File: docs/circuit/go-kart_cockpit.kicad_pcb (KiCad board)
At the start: 2 copper layers, 103.5 x 57.2 mm, 37 parts, among them P1 Power, Q1 TIP120, X1 Taster rechts (male), X10 Bluetooth-Modul, X11 Display (male), X12 PD7, X13 SDA, X14 PG4, X15 AVR-ISP-10, X16 Taster links (male), X17 Start/Stop/Rückwärts, X2 5V, X3 GND, X4 24V Hupe, X5 SCL, X6 CS, X7 PB6, X8 J5, X9 J3

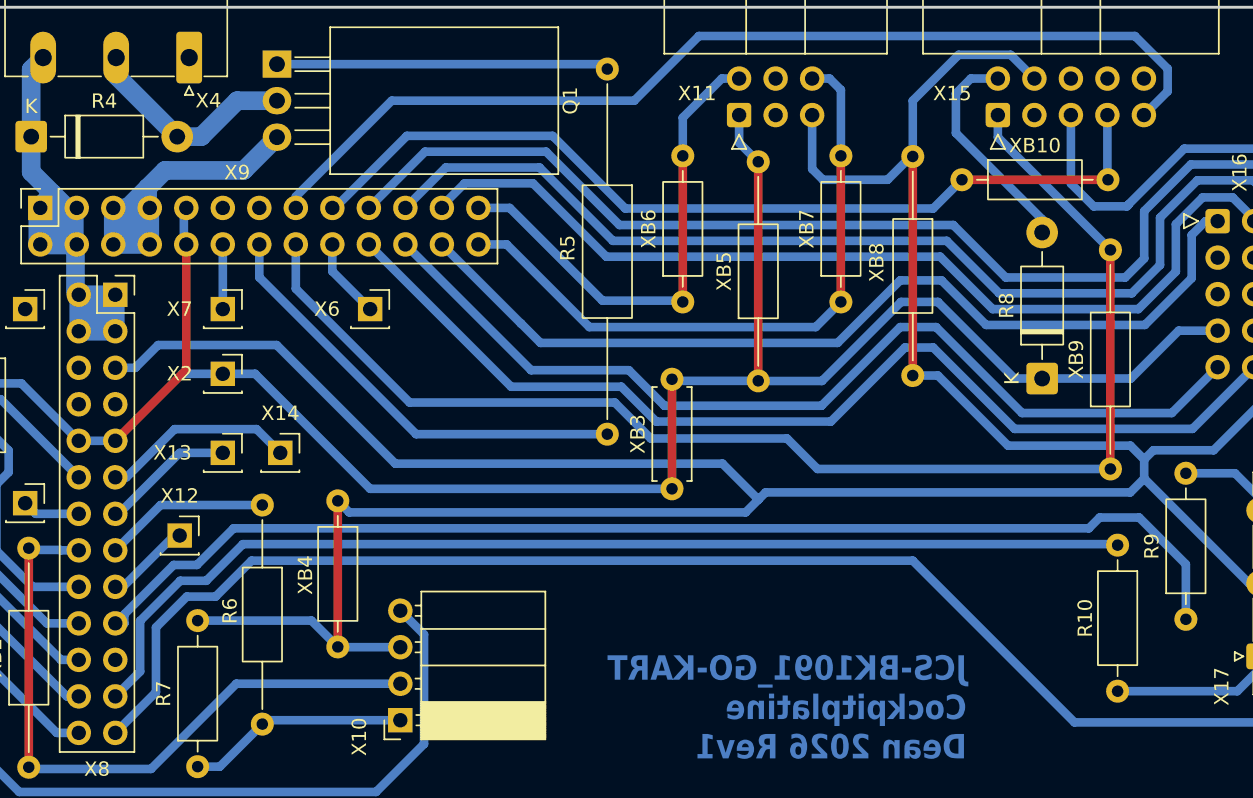
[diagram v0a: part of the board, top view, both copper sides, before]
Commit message: feat(PCB): add pull down resistor in preperation for FET
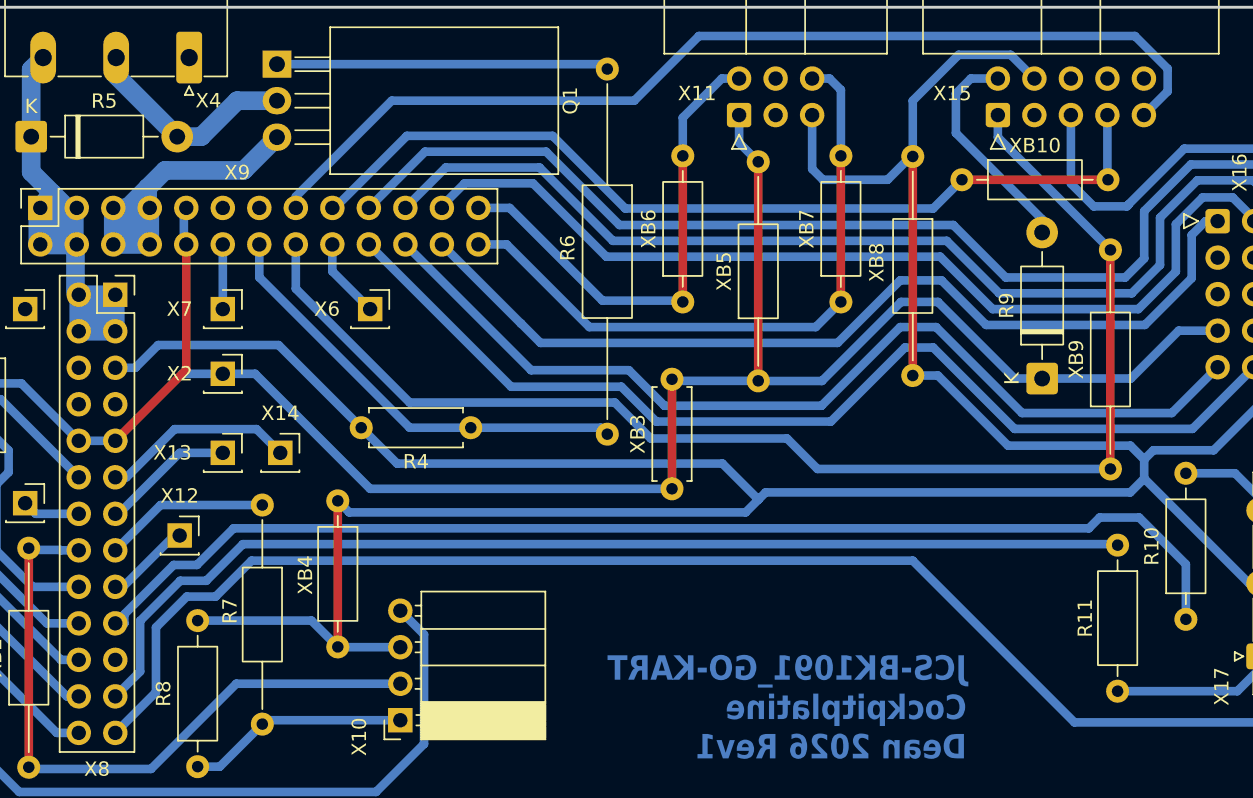
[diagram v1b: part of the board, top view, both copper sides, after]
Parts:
- added R4: 10k, Resistor_THT:R_Axial_DIN0207_L6.3mm_D2.5mm_P7.62mm_Horizontal, F.Cu at (98.5, 76.8)
- renumbered R9 to R10, R10 to R11, R4 to R5, R5 to R6, R6 to R7, R7 to R8, R8 to R9
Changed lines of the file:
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@@
 	(net 36 "/PG4")
 	(net 37 "/PB0_CS")
-	(net 38 "Net-(R8-A)")
-	(net 39 "Net-(R10-Pad2)")
+	(net 38 "Net-(R9-A)")
+	(net 39 "Net-(R11-Pad2)")
 	(net 40 "unconnected-(X1-Pin_4-Pad4)")
 	(net 41 "unconnected-(X1-Pin_6-Pad6)")
@@
 		(descr "Resistor, Axial_DIN0207 series, Axial, Horizontal, pin pitch=10.16mm, 0.25W = 1/4W, length*diameter=6.3*2.5mm^2, http://cdn-reichelt.de/documents/datenblatt/B400/1_4W%23YAG.pdf")
 		(tags "Resistor Axial_DIN0207 series Axial Horizontal pin pitch 10.16mm 0.25W = 1/4W length 6.3mm diameter 2.5mm")
-		(property "Reference" "R7"
+		(property "Reference" "R8"
 			(at 5.08 -2.37 90)
 			(layer "F.SilkS")
@@
 		(descr "Resistor, Axial_DIN0207 series, Axial, Horizontal, pin pitch=15.24mm, 0.25W = 1/4W, length*diameter=6.3*2.5mm^2, http://cdn-reichelt.de/documents/datenblatt/B400/1_4W%23YAG.pdf")
 		(tags "Resistor Axial_DIN0207 series Axial Horizontal pin pitch 15.24mm 0.25W = 1/4W length 6.3mm diameter 2.5mm")
-		(property "Reference" "R6"
+		(property "Reference" "R7"
 			(at 7.37 2.25 270)
 			(layer "F.SilkS")
@@
 		(descr "Diode, DO-41_SOD81 series, Axial, Horizontal, pin pitch=10.16mm, length*diameter=5.2*2.7mm^2, https://www.diodes.com/assets/Package-Files/DO-41-Plastic.pdf")
 		(tags "Diode DO-41_SOD81 series Axial Horizontal pin pitch 10.16mm  length 5.2mm diameter 2.7mm")
-		(property "Reference" "R4"
+		(property "Reference" "R5"
 			(at 5.08 -2.47 0)
 			(layer "F.SilkS")
@@
 		(descr "Resistor, Axial_DIN0207 series, Axial, Horizontal, pin pitch=10.16mm, 0.25W = 1/4W, length*diameter=6.3*2.5mm^2, http://cdn-reichelt.de/documents/datenblatt/B400/1_4W%23YAG.pdf")
 		(tags "Resistor Axial_DIN0207 series Axial Horizontal pin pitch 10.16mm 0.25W = 1/4W length 6.3mm diameter 2.5mm")
-		(property "Reference" "R10"
+		(property "Reference" "R11"
 			(at 5.08 2.25 270)
 			(layer "F.SilkS")
@@
 			(layers "*.Cu" "*.Mask")
 			(remove_unused_layers no)
-			(net 39 "Net-(R10-Pad2)")
+			(net 39 "Net-(R11-Pad2)")
 			(pintype "passive")
 		)
@@
 		(descr "Resistor, Axial_DIN0207 series, Axial, Horizontal, pin pitch=10.16mm, 0.25W = 1/4W, length*diameter=6.3*2.5mm^2, http://cdn-reichelt.de/documents/datenblatt/B400/1_4W%23YAG.pdf")
 		(tags "Resistor Axial_DIN0207 series Axial Horizontal pin pitch 10.16mm 0.25W = 1/4W length 6.3mm diameter 2.5mm")
-		(property "Reference" "R9"
+		(property "Reference" "R10"
 			(at 5.08 -2.37 90)
 			(layer "F.SilkS")
@@
 		(descr "Resistor, Axial_DIN0309 series, Axial, Horizontal, pin pitch=25.4mm, 0.5W = 1/2W, length*diameter=9*3.2mm^2, http://cdn-reichelt.de/documents/datenblatt/B400/1_4W%23YAG.pdf")
 		(tags "Resistor Axial_DIN0309 series Axial Horizontal pin pitch 25.4mm 0.5W = 1/2W length 9mm diameter 3.2mm")
-		(property "Reference" "R5"
+		(property "Reference" "R6"
 			(at 12.45 2.75 270)
 			(layer "F.SilkS")
@@
 			(remove_unused_layers no)
 			(roundrect_rratio 0.138889)
-			(net 39 "Net-(R10-Pad2)")
+			(net 39 "Net-(R11-Pad2)")
 			(pinfunction "1")
 			(pintype "passive")
@@
 		)
 	)
+	(footprint "Resistor_THT:R_Axial_DIN0207_L6.3mm_D2.5mm_P7.62mm_Horizontal"
+		(layer "F.Cu")
+		(at 98.5 76.75 180)
+		(descr "Resistor, Axial_DIN0207 series, Axial, Horizontal, pin pitch=7.62mm, 0.25W = 1/4W, length*diameter=6.3*2.5mm^2, http://cdn-reichelt.de/documents/datenblatt/B400/1_4W%23YAG.pdf")
+		(tags "Resistor Axial_DIN0207 series Axial Horizontal pin pitch 7.62mm 0.25W = 1/4W length 6.3mm diameter 2.5mm")
+		(property "Reference" "R4"
+			(at 3.81 -2.37 0)
+			(layer "F.SilkS")
+			(effects
+				(font
+					(size 1 1)
+					(thickness 0.15)
+				)
+			)
+		)
+		(property "Value" "10k"
+			(at 3.81 2.37 0)
+			(layer "F.Fab")
+			(effects
+				(font
+					(size 1 1)
+					(thickness 0.15)
+				)
+			)
+		)
+		(property "Datasheet" "~"
+			(at 0 0 0)
+			(layer "F.Fab")
+			(hide yes)
+			(effects
+				(font
+					(size 1.27 1.27)
+					(thickness 0.15)
+				)
+			)
+		)
+		(property "Description" "Resistor"
+			(at 0 0 0)
+			(layer "F.Fab")
+			(hide yes)
+			(effects
+				(font
+					(size 1.27 1.27)
+					(thickness 0.15)
+				)
+			)
+		)
+		(property ki_fp_filters "R_*")
+		(sheetname "/")
+		(sheetfile "go-kart_cockpit.kicad_sch")
+		(attr through_hole)
+		(fp_line
+			(start 7.08 1.37)
+			(end 7.08 1.04)
+			(stroke
+				(width 0.12)
+				(type solid)
+			)
+			(layer "F.SilkS")
+		)
+		(fp_line
+			(start 7.08 -1.37)
+			(end 7.08 -1.04)
+			(stroke
+				(width 0.12)
+				(type solid)
+			)
+			(layer "F.SilkS")
+		)
+		(fp_line
+			(start 0.54 1.37)
+			(end 7.08 1.37)
+			(stroke
+				(width 0.12)
+				(type solid)
+			)
+			(layer "F.SilkS")
+		)
+		(fp_line
+			(start 0.54 1.04)
+			(end 0.54 1.37)
+			(stroke
+				(width 0.12)
+				(type solid)
+			)
+			(layer "F.SilkS")
+		)
+		(fp_line
+			(start 0.54 -1.04)
+			(end 0.54 -1.37)
+			(stroke
+				(width 0.12)
+				(type solid)
+			)
+			(layer "F.SilkS")
+		)
+		(fp_line
+			(start 0.54 -1.37)
+			(end 7.08 -1.37)
+			(stroke
+				(width 0.12)
+				(type solid)
+			)
+			(layer "F.SilkS")
+		)
+		(fp_rect
+			(start -1.05 -1.5)
+			(end 8.67 1.5)
+			(stroke
+				(width 0.05)
+				(type solid)
+			)
+			(fill no)
+			(layer "F.CrtYd")
+		)
+		(fp_line
+			(start 7.62 0)
+			(end 6.96 0)
+			(stroke
+				(width 0.1)
+				(type solid)
+			)
+			(layer "F.Fab")
+		)
+		(fp_line
+			(start 0 0)
+			(end 0.66 0)
+			(stroke
+				(width 0.1)
+				(type solid)
+			)
+			(layer "F.Fab")
+		)
+		(fp_rect
+			(start 0.66 -1.25)
+			(end 6.96 1.25)
+			(stroke
+				(width 0.1)
+				(type solid)
+			)
+			(fill no)
+			(layer "F.Fab")
+		)
+		(fp_text user "${REFERENCE}"
+			(at 3.81 0 0)
+			(layer "F.Fab")
+			(effects
+				(font
+					(size 1 1)
+					(thickness 0.15)
+				)
+			)
+		)
+		(pad "1" thru_hole circle
+			(at 0 0 180)
+			(size 1.6 1.6)
+			(drill 0.8)
+			(layers "*.Cu" "*.Mask")
+			(remove_unused_layers no)
+			(net 30 "PB4_OC2A")
+			(pintype "passive")
+		)
+		(pad "2" thru_hole circle
+			(at 7.62 0 180)
+			(size 1.6 1.6)
+			(drill 0.8)
+			(layers "*.Cu" "*.Mask")
+			(remove_unused_layers no)
+			(net 2 "GND")
+			(pintype "passive")
+		)
+		(embedded_fonts no)
+		(model "${KICAD9_3DMODEL_DIR}/Resistor_THT.3dshapes/R_Axial_DIN0207_L6.3mm_D2.5mm_P7.62mm_Horizontal.step"
+			(offset
+				(xyz 0 0 0)
+			)
+			(scale
+				(xyz 1 1 1)
+			)
+			(rotate
+				(xyz 0 0 0)
+			)
+		)
+	)
 	(footprint "Diode_THT:D_DO-41_SOD81_P10.16mm_Horizontal"
 		(layer "F.Cu")
@@
 		(descr "Diode, DO-41_SOD81 series, Axial, Horizontal, pin pitch=10.16mm, length*diameter=5.2*2.7mm^2, https://www.diodes.com/assets/Package-Files/DO-41-Plastic.pdf")
 		(tags "Diode DO-41_SOD81 series Axial Horizontal pin pitch 10.16mm  length 5.2mm diameter 2.7mm")
-		(property "Reference" "R8"
+		(property "Reference" "R9"
 			(at 5.08 -2.47 90)
 			(layer "F.SilkS")
@@
 			(layers "*.Cu" "*.Mask")
 			(remove_unused_layers no)
-			(net 38 "Net-(R8-A)")
+			(net 38 "Net-(R9-A)")
 			(pinfunction "A")
 			(pintype "passive")
@@
 			(layers "*.Cu" "*.Mask")
 			(remove_unused_layers no)
-			(net 38 "Net-(R8-A)")
+			(net 38 "Net-(R9-A)")
 			(pinfunction "VCC")
 			(pintype "passive")
@@
 	)
 	(segment
-		(start 93.25 79.25)
-		(end 85 71)
+		(start 154.651 71.651)
+		(end 154.651 73.849)
 		(width 0.6)
 		(layer "B.Cu")
@@
 	)
 	(segment
-		(start 154.651 71.651)
-		(end 154.651 73.849)
+		(start 116.009156 79.245)
+		(end 118.514156 81.75)
 		(width 0.6)
 		(layer "B.Cu")
@@
 	)
 	(segment
+		(start 90.88 76.75)
+		(end 85.13 71)
+		(width 0.6)
+		(layer "B.Cu")
+		(net 2)
+	)
+	(segment
 		(start 64.71 78.96)
 		(end 64.75 79)
@@
 	)
 	(segment
-		(start 85 71)
-		(end 76.75 71)
-		(width 0.6)
-		(layer "B.Cu")
-		(net 2)
-	)
-	(segment
 		(start 154.651 73.849)
 		(end 150.181 78.319)
@@
 	)
 	(segment
-		(start 76.75 71)
-		(end 75.17 72.58)
-		(width 0.6)
+		(start 73.63 64)
+		(end 76.17 61.46)
+		(width 1.3)
 		(layer "B.Cu")
 		(net 2)
 	)
 	(segment
-		(start 73.63 64)
-		(end 76.17 61.46)
-		(width 1.3)
+		(start 76.75 71)
+		(end 75.17 72.58)
+		(width 0.6)
 		(layer "B.Cu")
 		(net 2)
@@
 	)
 	(segment
-		(start 116.014156 79.25)
-		(end 93.25 79.25)
+		(start 65 71.5)
+		(end 65 71.44)
 		(width 0.6)
 		(layer "B.Cu")
@@
 	)
 	(segment
-		(start 65 71.5)
-		(end 65 71.44)
+		(start 93.375 79.245)
+		(end 116.009156 79.245)
 		(width 0.6)
 		(layer "B.Cu")
@@
 	)
 	(segment
-		(start 118.514156 81.75)
-		(end 116.014156 79.25)
-		(width 0.6)
-		(layer "B.Cu")
-		(net 2)
-	)
-	(segment
 		(start 150.181 78.319)
 		(end 145.988844 78.319)
@@
 	)
 	(segment
+		(start 90.88 76.75)
+		(end 93.375 79.245)
+		(width 0.6)
+		(layer "B.Cu")
+		(net 2)
+	)
+	(segment
 		(start 119.014156 81.25)
 		(end 118.514156 81.75)
@@
 	)
 	(segment
+		(start 85.13 71)
+		(end 76.75 71)
+		(width 0.6)
+		(layer "B.Cu")
+		(net 2)
+	)
+	(segment
 		(start 71.23 72.58)
 		(end 71.15 72.5)
@@
 	)
 	(segment
+		(start 75.17 72.58)
+		(end 73.77 72.58)
+		(width 0.6)
+		(layer "B.Cu")
+		(net 2)
+	)
+	(segment
 		(start 82.709 58.851)
 		(end 77.227 58.851)
@@
 	)
 	(segment
-		(start 75.17 72.58)
-		(end 73.77 72.58)
-		(width 0.6)
-		(layer "B.Cu")
-		(net 2)
-	)
-	(segment
 		(start 85.14 51.34)
 		(end 85.02 51.46)
@@
 	)
 	(segment
-		(start 83.79 64)
+		(start 107.55 76.75)
+		(end 108 77.2)
+		(width 0.6)
+		(layer "B.Cu")
+		(net 30)
+	)
+	(segment
+		(start 94.25 76.75)
 		(end 83.79 66.29)
 		(width 0.6)
@@
 	(segment
 		(start 83.79 66.29)
-		(end 94.7 77.2)
+		(end 83.79 64)
 		(width 0.6)
 		(layer "B.Cu")
@@
 	)
 	(segment
-		(start 94.7 77.2)
-		(end 108 77.2)
+		(start 98.5 76.75)
+		(end 94.25 76.75)
+		(width 0.6)
+		(layer "B.Cu")
+		(net 30)
+	)
+	(segment
+		(start 98.5 76.75)
+		(end 107.55 76.75)
 		(width 0.6)
 		(layer "B.Cu")

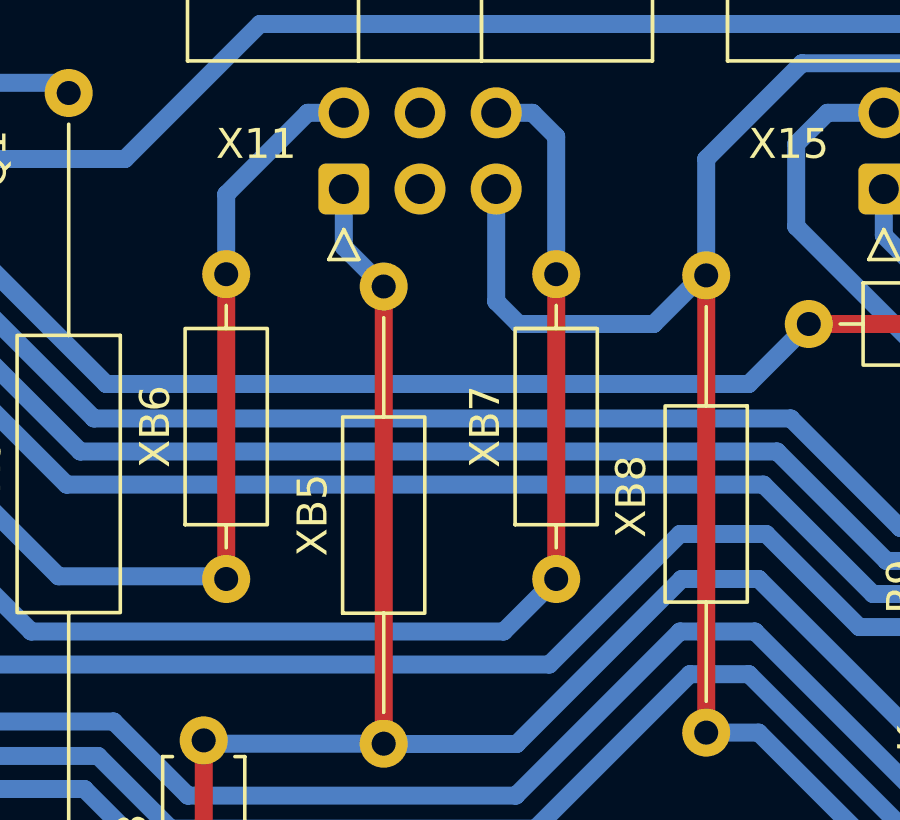
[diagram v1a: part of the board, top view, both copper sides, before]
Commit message: feat(PCB): add teardrops
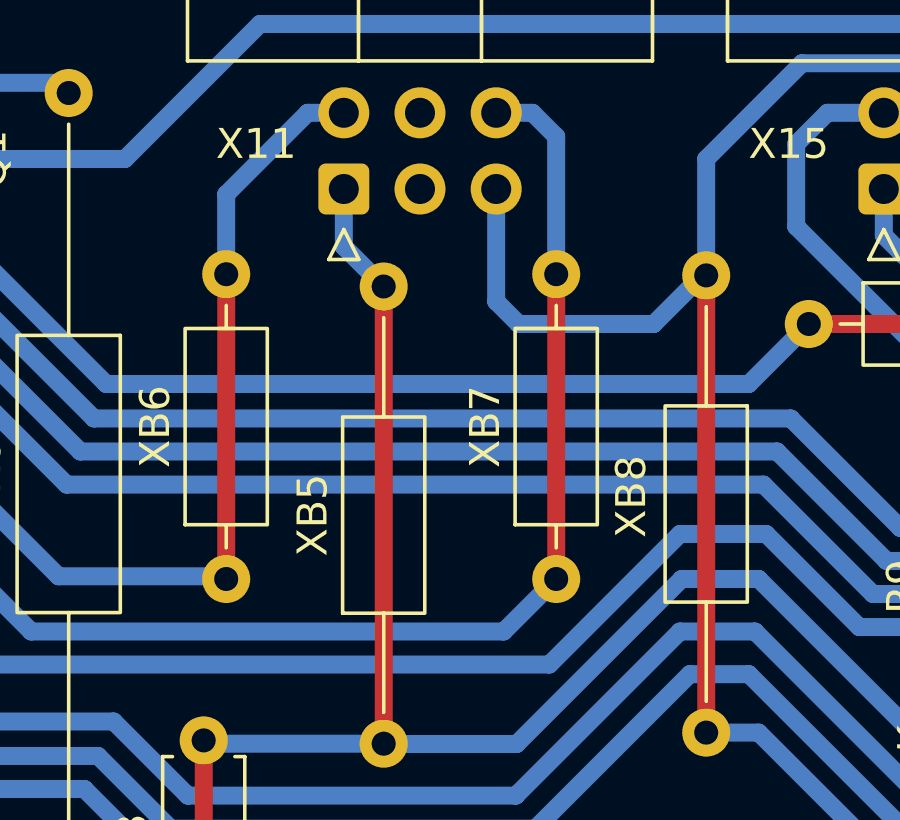
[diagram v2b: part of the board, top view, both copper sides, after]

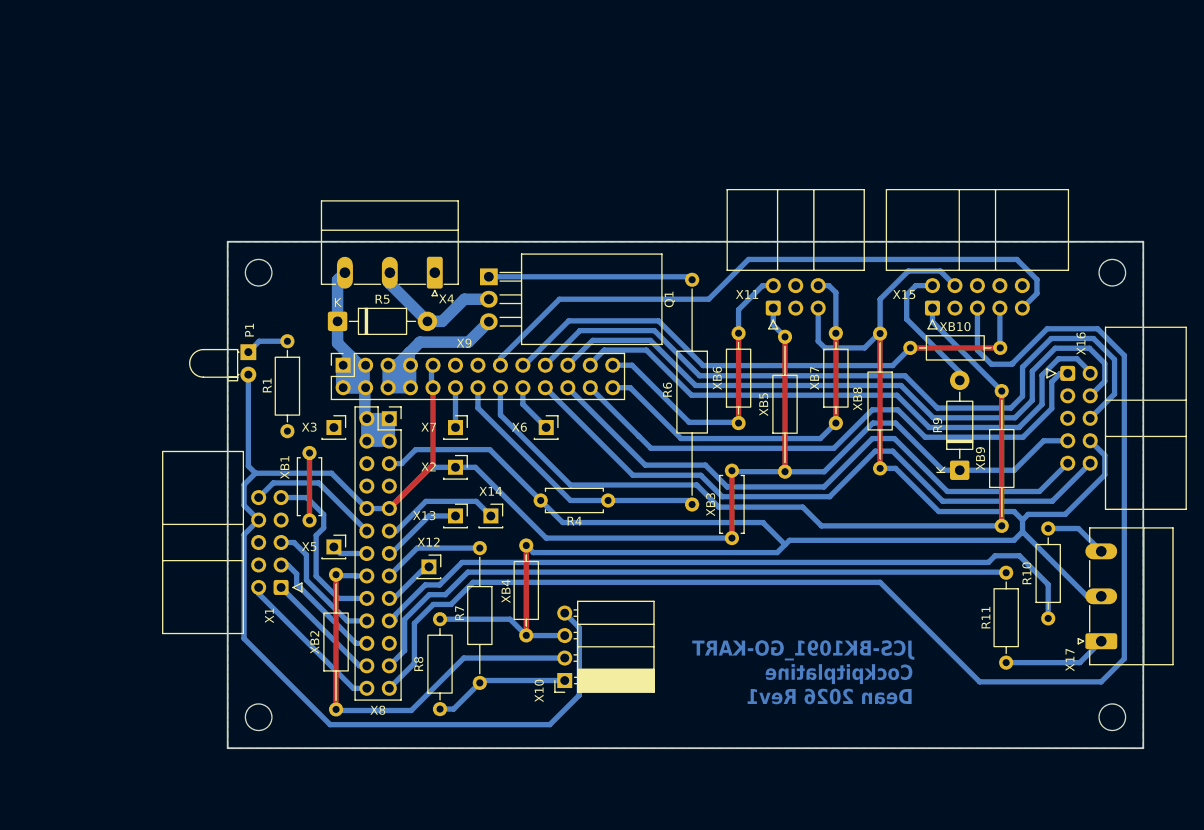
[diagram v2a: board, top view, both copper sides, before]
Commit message: feat(PCB): improve connectors and position
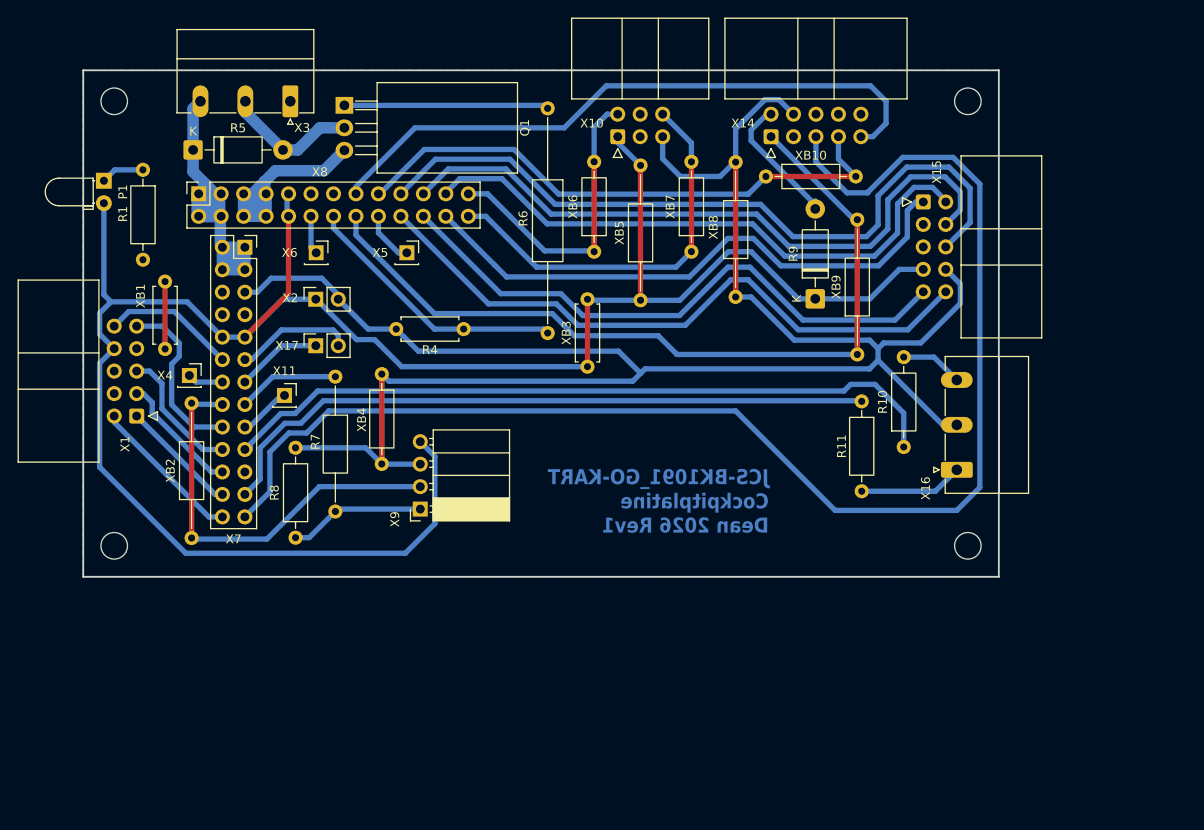
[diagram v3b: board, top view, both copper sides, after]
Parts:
- removed X13: SDA, Connector_PinSocket_2.54mm:PinSocket_1x01_P2.54mm_Vertical
- removed the X14 at (85.2, 78.5)
- removed the X3 at (67.5, 68.5)
- added X17: SDA PG4, Connector_PinSocket_2.54mm:PinSocket_1x02_P2.54mm_Vertical, F.Cu at (65.5, 59.2)
- X2: value 5V -> 5V GND; footprint Connector_PinSocket_2.54mm:PinSocket_1x01_P2.54mm_Vertical -> Connector_PinSocket_2.54mm:PinSocket_1x02_P2.54mm_Vertical
- moved X14 26.6 mm to (116.9, 35.6)
- moved X10 26.2 mm to (99.6, 35.6)
- moved R10 25.3 mm to (131.9, 70.7)
- moved X15 25.3 mm to (134.1, 43.0)
- moved R11 25.3 mm to (127.2, 65.5)
- moved R8 25.3 mm to (63.2, 81.0)
- moved X1 25.3 mm to (45.2, 67.2)
- moved X11 25.3 mm to (61.9, 64.9)
- moved X16 25.3 mm to (137.9, 73.3)
- moved XB2 25.3 mm to (51.4, 81.0)
- moved XB4 25.3 mm to (72.9, 62.5)
- moved XB8 25.3 mm to (112.9, 38.5)
- moved XB9 25.3 mm to (126.7, 60.2)
- moved P1 25.3 mm to (41.5, 40.6)
- moved Q1 25.3 mm to (68.7, 32.1)
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- renumbered X11 to X10, X12 to X11, X15 to X14, X16 to X15, X17 to X16, X4 to X3, X5 to X4, X6 to X5, X7 to X6, X8 to X7, X9 to X8, X10 to X9
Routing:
- net PB3_MISO: track 70.9 -> 72.1 mm
- net GND: track 261.4 -> 260.2 mm
- net /RESET: track 155.7 -> 156.5 mm
- net PB1_SCK: track 63.5 -> 64.3 mm
- net /PD1_SDA: track 9.24 -> 9.96 mm
- net PB4_OC2A: track 31.0 -> 30.5 mm
- net PE1_TXD0: track 35.2 -> 34.6 mm
